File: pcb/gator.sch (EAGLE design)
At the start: 81 parts, among them J2 POWER_JACKPTH, X1 USB-A-S, Y1 12MHz

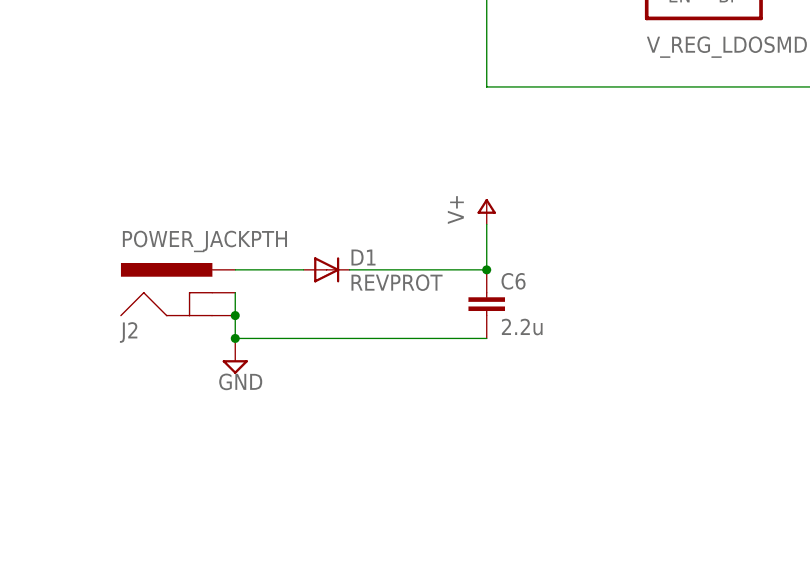
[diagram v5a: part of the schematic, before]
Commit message: Routed and cleaned up USB power, SD card signals, ethernet phy
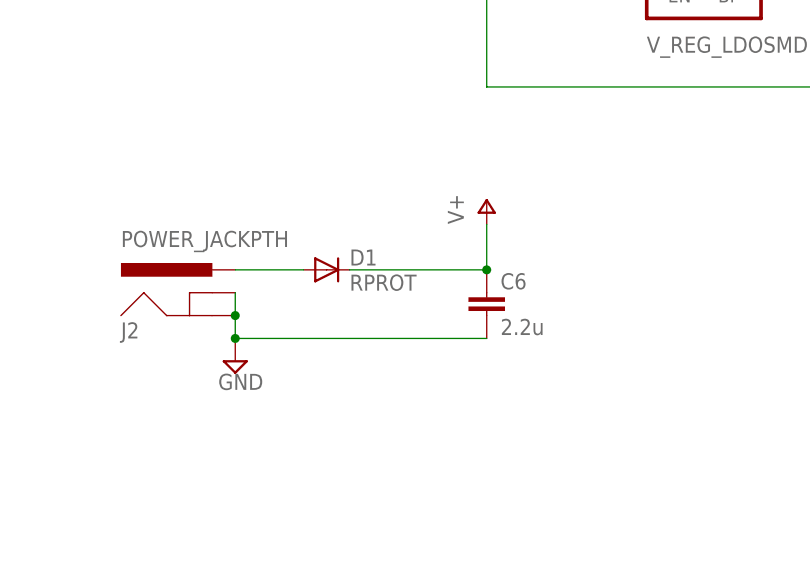
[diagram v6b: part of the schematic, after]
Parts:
- D1: value REVPROT -> RPROT
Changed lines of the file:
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@@
 <?xml version="1.0" encoding="utf-8"?>
 <!DOCTYPE eagle SYSTEM "eagle.dtd">
-<eagle version="6.2">
+<eagle version="6.3">
 <drawing>
 <settings>
@@
 <part name="C6" library="SparkFun-Passives" deviceset="CAP" device="0603-CAP" value="2.2u"/>
 <part name="P+4" library="supply1" deviceset="V+" device=""/>
-<part name="D1" library="SparkFun-DiscreteSemi" deviceset="DIODE" device="PTH" value="REVPROT"/>
+<part name="D1" library="SparkFun-DiscreteSemi" deviceset="DIODE" device="PTH" value="RPROT"/>
 <part name="MIC5219-3.3YM5_1" library="SparkFun-PowerIC" deviceset="V_REG_LDO" device="SMD"/>
 <part name="C7" library="SparkFun-Passives" deviceset="CAP" device="0603-CAP" value="470p"/>

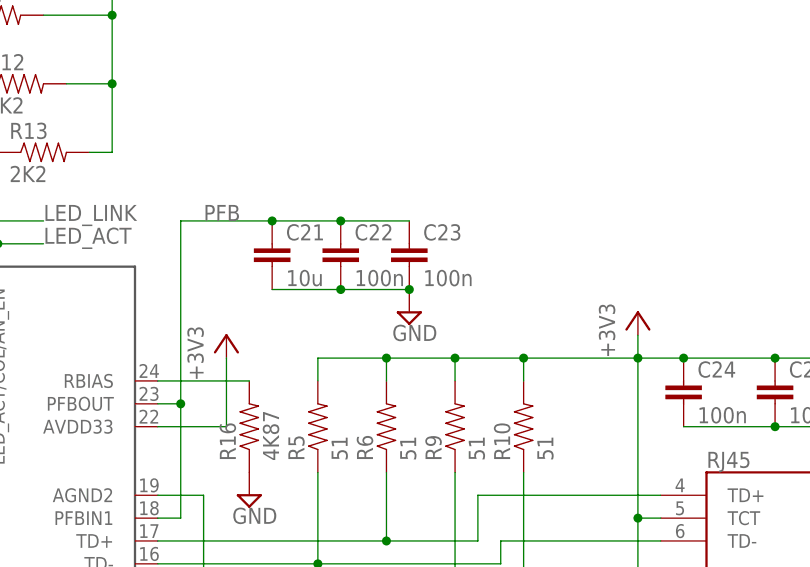
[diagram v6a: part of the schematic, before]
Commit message: Finished routing ethernet
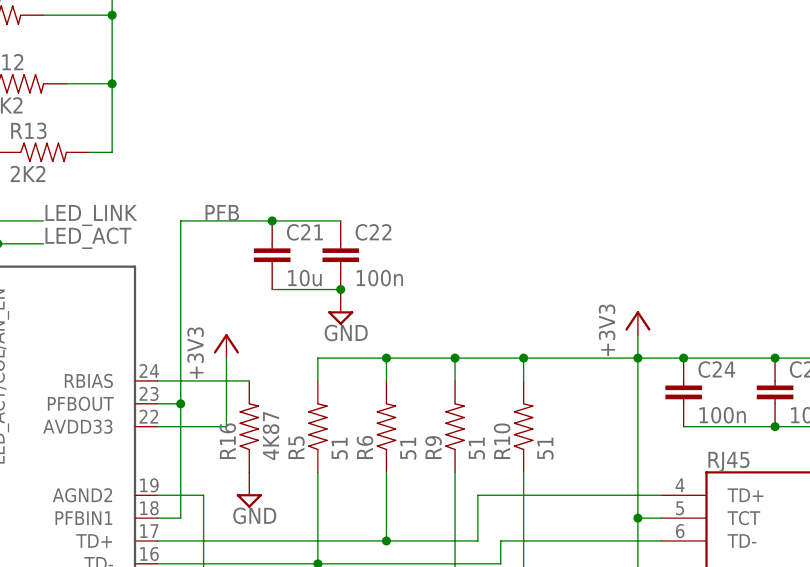
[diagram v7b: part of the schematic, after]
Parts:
- removed C23: 100n, SparkFun-Passives:CAP0603-CAP
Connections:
- net GND: no longer C23.2
- net PFB: no longer C23.1
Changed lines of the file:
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@@
 <part name="C21" library="SparkFun-Passives" deviceset="CAP" device="0603-CAP" value="10u"/>
 <part name="C22" library="SparkFun-Passives" deviceset="CAP" device="0603-CAP" value="100n"/>
-<part name="C23" library="SparkFun-Passives" deviceset="CAP" device="0603-CAP" value="100n"/>
 <part name="R16" library="SparkFun-Passives" deviceset="RESISTOR" device="0603-RES" value="4K87"/>
 <part name="SUPPLY16" library="supply2" deviceset="GND" device=""/>
@@
 <instance part="C21" gate="G$1" x="-101.6" y="309.88"/>
 <instance part="C22" gate="G$1" x="-93.98" y="309.88"/>
-<instance part="C23" gate="G$1" x="-86.36" y="309.88"/>
 <instance part="R16" gate="G$1" x="-104.14" y="292.1" rot="R90"/>
 <instance part="SUPPLY16" gate="GND" x="-104.14" y="284.48"/>
-<instance part="SUPPLY17" gate="GND" x="-86.36" y="304.8"/>
+<instance part="SUPPLY17" gate="GND" x="-93.98" y="304.8"/>
 <instance part="+3V11" gate="G$1" x="-106.68" y="302.26"/>
 <instance part="+3V12" gate="G$1" x="-147.32" y="325.12"/>
@@
 </segment>
 <segment>
-<pinref part="C23" gate="G$1" pin="2"/>
 <pinref part="SUPPLY17" gate="GND" pin="GND"/>
 <pinref part="C21" gate="G$1" pin="2"/>
-<wire x1="-86.36" y1="307.34" x2="-93.98" y2="307.34" width="0.1524" layer="91"/>
 <pinref part="C22" gate="G$1" pin="2"/>
 <junction x="-93.98" y="307.34"/>
 <wire x1="-93.98" y1="307.34" x2="-101.6" y2="307.34" width="0.1524" layer="91"/>
-<junction x="-86.36" y="307.34"/>
 </segment>
 <segment>
@@
 <wire x1="-114.3" y1="294.64" x2="-111.76" y2="294.64" width="0.1524" layer="91"/>
 <wire x1="-111.76" y1="294.64" x2="-111.76" y2="314.96" width="0.1524" layer="91"/>
-<pinref part="C23" gate="G$1" pin="1"/>
 <wire x1="-111.76" y1="314.96" x2="-101.6" y2="314.96" width="0.1524" layer="91"/>
 <pinref part="ETH_PHY" gate="G$1" pin="PFBIN1"/>
 <wire x1="-101.6" y1="314.96" x2="-93.98" y2="314.96" width="0.1524" layer="91"/>
-<wire x1="-93.98" y1="314.96" x2="-86.36" y2="314.96" width="0.1524" layer="91"/>
 <wire x1="-114.3" y1="281.94" x2="-111.76" y2="281.94" width="0.1524" layer="91"/>
 <wire x1="-111.76" y1="281.94" x2="-111.76" y2="294.64" width="0.1524" layer="91"/>
@@
 <junction x="-101.6" y="314.96"/>
 <pinref part="C22" gate="G$1" pin="1"/>
-<junction x="-93.98" y="314.96"/>
 <label x="-109.22" y="314.96" size="1.778" layer="95"/>
 </segment>

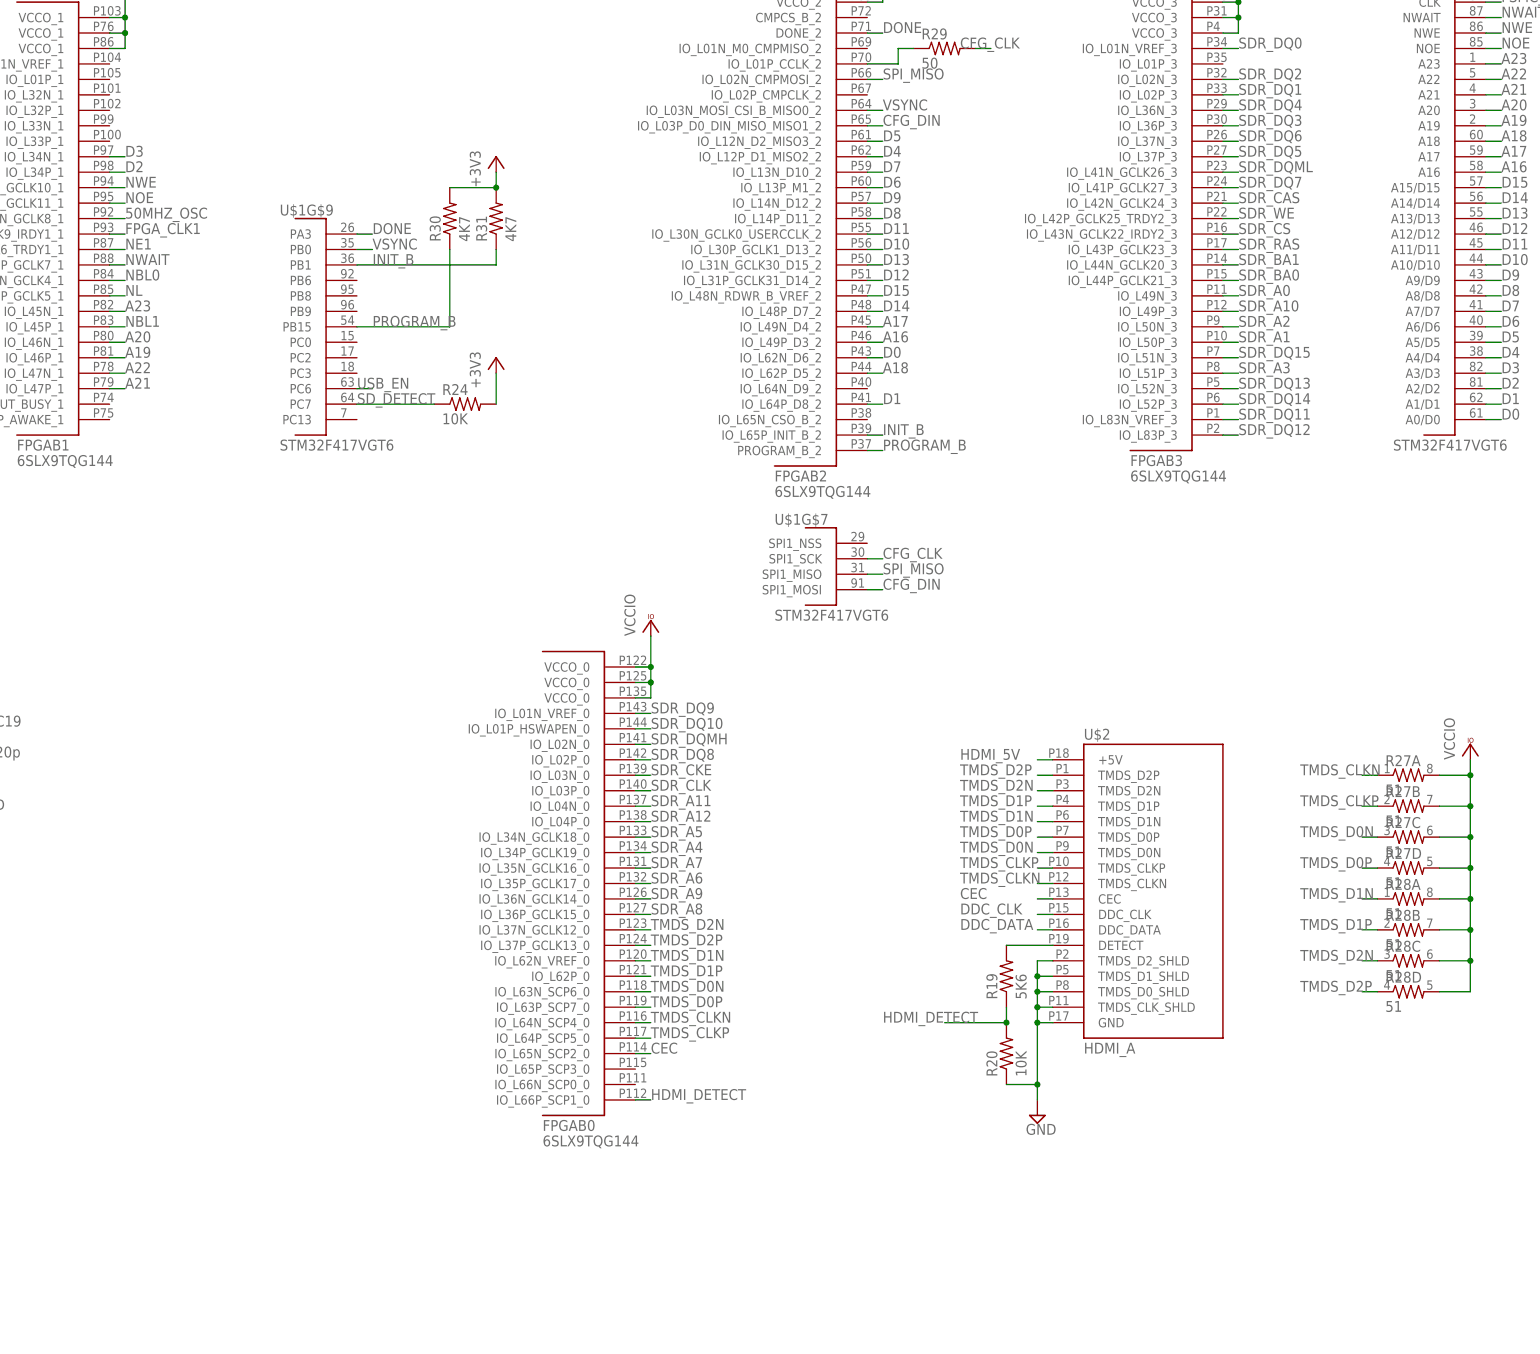
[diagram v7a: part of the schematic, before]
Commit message: Finished routing CEC, DDC, and remaining power; still have to do decoupling caps
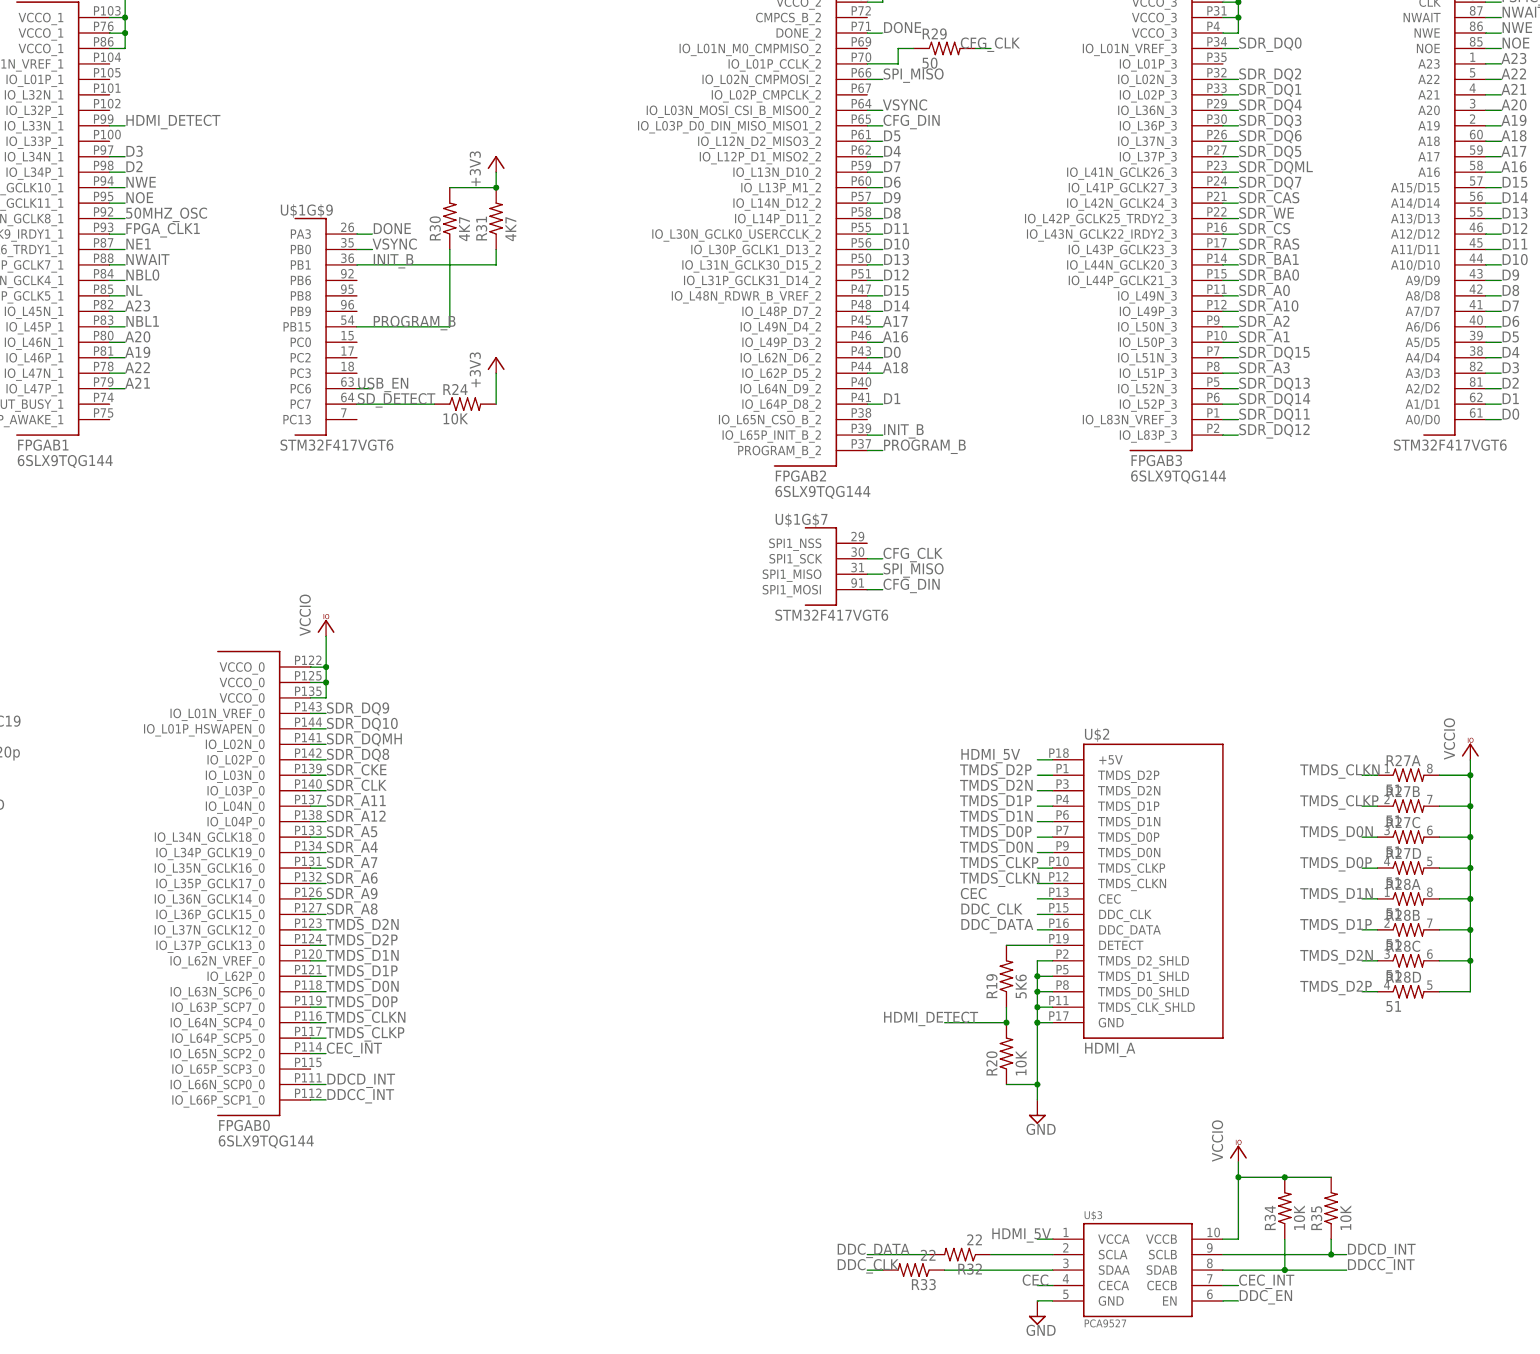
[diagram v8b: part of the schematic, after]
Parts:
- added R32, R33: 22, SparkFun-Passives:RESISTOR0603-RES
- added R34, R35: 10K, SparkFun-Passives:RESISTOR0603-RES
- added U$3: PCA9527, gator:PCA9527
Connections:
- new net CEC_INT: FPGAB0.IO_L65N_SCP2_0, U$3.CECB
- new net DDCC_INT: FPGAB0.IO_L66P_SCP1_0, R34.1, U$3.SDAB
- new net DDCD_INT: FPGAB0.IO_L66N_SCP0_0, R35.1, U$3.SCLB
- new net DDC_EN: U$3.EN
- new net N$10: R33.1, U$3.SDAA
- new net N$9: R32.1, U$3.SCLA
- net CEC: now also U$3.CECA; no longer FPGAB0.IO_L65N_SCP2_0
- net DDC_CLK: now also R33.2
- net DDC_DATA: now also R32.2
- net GND: now also U$3.GND@5
- net HDMI_5V: now also U$3.VCCA
- net HDMI_DETECT: now also FPGAB1.IO_L33N_1; no longer FPGAB0.IO_L66P_SCP1_0
- net VCCIO: now also R34.2, R35.2, U$3.VCCB
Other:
- moved on the sheet: FPGAB0
